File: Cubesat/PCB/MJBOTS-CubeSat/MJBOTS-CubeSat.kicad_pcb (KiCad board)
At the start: 2 copper layers, 88 x 73 mm, 11 parts, among them J1 Li 24V Battery, J2 MPU 6050, J3 Conn_01x08, J4 Conn_02x20_Odd_Even, U1 LM2596S

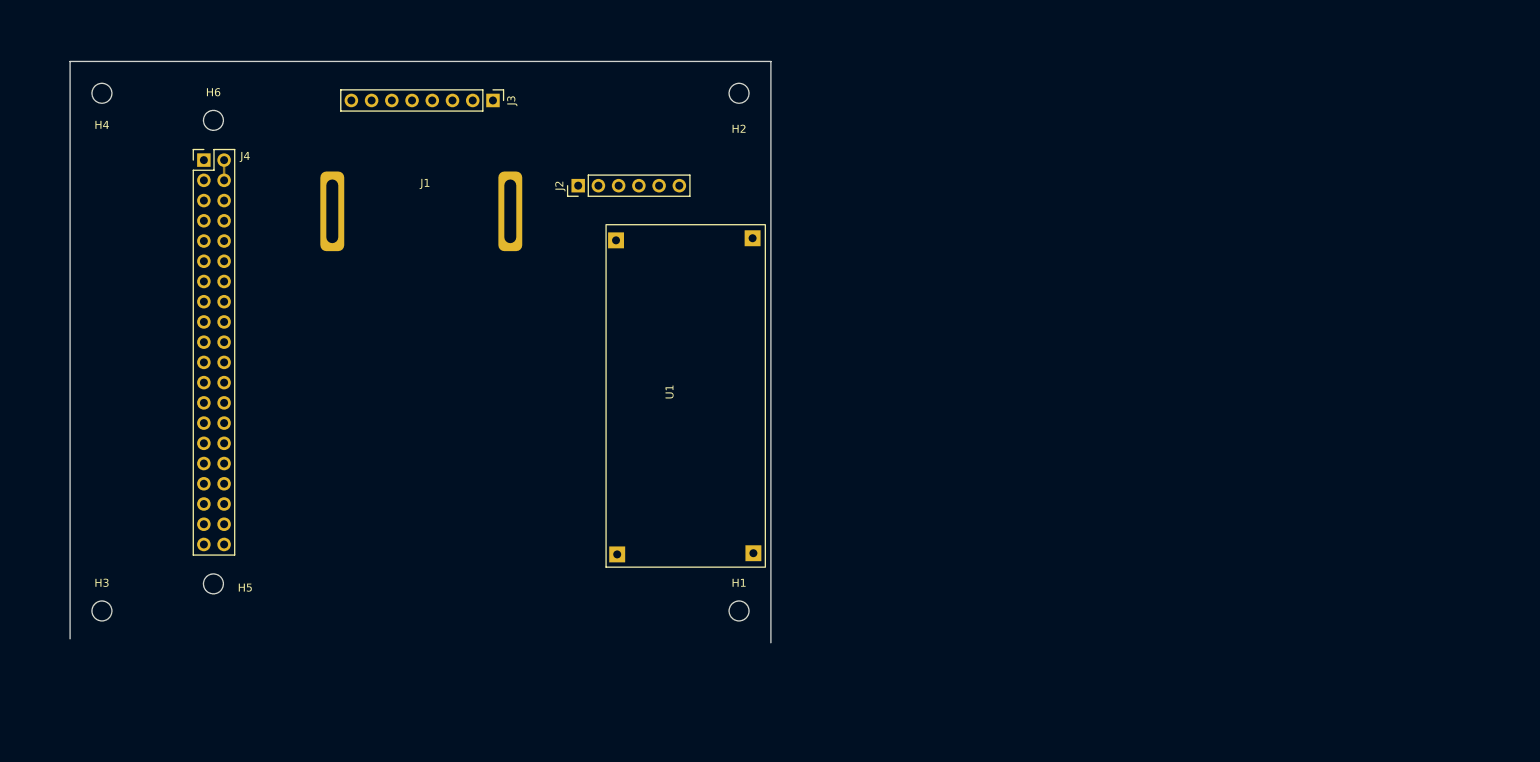
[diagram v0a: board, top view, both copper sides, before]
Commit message: Updated Moteus PCB
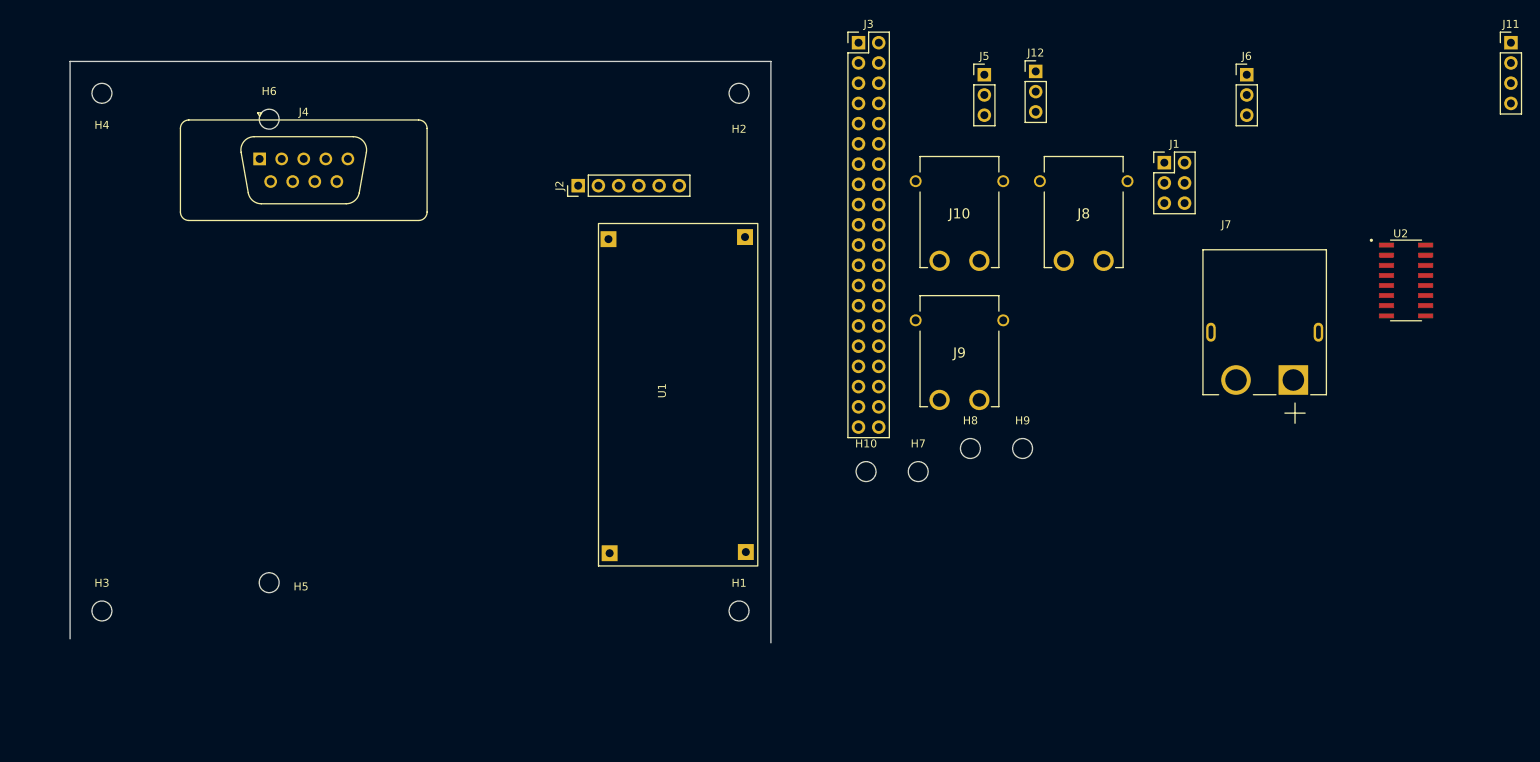
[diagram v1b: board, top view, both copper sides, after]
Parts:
- added H10: MountingHole, MountingHole:MountingHole_2.5mm, F.Cu at (194.9, 96.5)
- added H7: MountingHole, MountingHole:MountingHole_2.5mm, F.Cu at (201.5, 96.5)
- added H8: MountingHole, MountingHole:MountingHole_2.5mm, F.Cu at (208.1, 93.6)
- added H9: MountingHole, MountingHole:MountingHole_2.5mm, F.Cu at (214.6, 93.6)
- added J10: MOTOR3-XT30, cube:XT30PWM, F.Cu at (206.7, 64.1)
- added J11: JST-BATT, Connector_PinHeader_2.54mm:PinHeader_1x04_P2.54mm_Vertical, F.Cu at (275.9, 42.6)
- added J12: MOTOR3, Connector_PinHeader_2.54mm:PinHeader_1x03_P2.54mm_Vertical, F.Cu at (216.2, 46.2)
- added J5: MOTOR1, Connector_PinHeader_2.54mm:PinHeader_1x03_P2.54mm_Vertical, F.Cu at (209.8, 46.7)
- added J6: MOTOR2, Connector_PinHeader_2.54mm:PinHeader_1x03_P2.54mm_Vertical, F.Cu at (242.8, 46.7)
- added J7: INPUT-XT60, cube:AMASS_XT60PW-M, F.Cu at (245.0, 79.0)
- added J8: MOTOR1-XT30, cube:XT30PWM, F.Cu at (222.3, 64.1)
- added J9: MOTOR2-XT30, cube:XT30PWM, F.Cu at (206.7, 81.6)
- added U2: MCP3008-I/SL, cube:SOIC127P600X175-16N, F.Cu at (262.8, 72.5)
- J1: value Li 24V Battery -> Display; footprint cube:24V_Li_batt -> Connector_PinHeader_2.54mm:PinHeader_2x03_P2.54mm_Vertical
- J3: value Conn_01x08 -> Pi_GPIO; footprint Connector_PinHeader_2.54mm:PinHeader_1x08_P2.54mm_Vertical -> Connector_PinHeader_2.54mm:PinHeader_2x20_P2.54mm_Vertical
- J4: value Conn_02x20_Odd_Even -> CAN; footprint Connector_PinHeader_2.54mm:PinHeader_2x20_P2.54mm_Vertical -> Connector_Dsub:DSUB-9_Male_Vertical_P2.77x2.84mm
- moved J1 102.4 mm to (232.4, 57.7)
- moved J3 46.5 mm to (194.0, 42.6), turned to 0 degrees
- moved H5 7.00 mm to (120.0, 110.5)
- moved H6 7.00 mm to (120.0, 52.2)
- moved J4 7.00 mm to (118.8, 57.2)
- moved U1 0.96 mm to (171.2, 86.2)
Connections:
- J3 pad 1: VCC -> /3.3V
- J3 pad 2: GND -> /5V
- J3 pad 3: /brake -> /SDA
- J3 pad 4: /PWM -> /5V
- J3 pad 5: /CW/CCW -> /SCL
- J3 pad 6: unconnected-(J3-Pad6) -> GND
- J3 pad 7: /CHB -> unconnected-(J3-Pad7)
- J3 pad 8: /CHA -> unconnected-(J3-Pad8)
- J4 pad 1: /3.3V -> unconnected-(J4-Pad1)
- J4 pad 2: /5VB -> /CAN_L
- J4 pad 3: /SDA -> GND
- J4 pad 4: /5VB -> unconnected-(J4-Pad4)
- J4 pad 5: /SCL -> unconnected-(J4-Pad5)
- J4 pad 6: GND -> unconnected-(J4-Pad6)
- J4 pad 7: unconnected-(J4-Pad7) -> /CAN_H
- U1 pad 1: VCC -> /VCC
- U1 pad 3: /5VB -> /5V
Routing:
- net /5VB: track 2.54 -> 0.00 mm

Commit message: Updated CubeSat PCB
Still need the dimensions for the CAN bus converter
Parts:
- removed H5: MountingHole, MountingHole:MountingHole_2.5mm
- U2: moved to B.Cu
- moved J11 170.0 mm to (106.0, 47.6), turned to 90 degrees
- moved U2 155.2 mm to (107.7, 80.2), turned to -90 degrees
- moved J1 126.2 mm to (118.9, 112.9)
- moved J7 112.4 mm to (135.0, 56.1)
- moved J6 100.2 mm to (167.3, 112.6), turned to -90 degrees
- moved J10 87.6 mm to (133.9, 112.9), turned to 180 degrees
- moved J12 86.8 mm to (167.3, 118.0), turned to -90 degrees
- moved J8 86.3 mm to (151.2, 113.0), turned to 180 degrees
- moved J3 76.4 mm to (118.9, 57.1)
- moved H7 72.6 mm to (129.8, 84.8)
- moved H10 65.1 mm to (129.9, 97.0)
- moved J9 61.0 mm to (152.5, 53.6)
- moved H9 59.5 mm to (155.2, 97.5)
- moved H8 53.5 mm to (155.2, 85.3)
- moved J5 39.2 mm to (170.6, 47.9), turned to -90 degrees
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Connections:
- J3 pad 22: /CS -> unconnected-(J3-Pad22)
- J3 pad 24: /SCLK -> /CS
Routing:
- net /3.3V: track 0.00 -> 130.4 mm
- net /SDA: track 0.00 -> 123.0 mm
- net /SCL: track 0.00 -> 120.9 mm
- net /5V: track 0.00 -> 103.4 mm
- net /CAN_H: track 0.00 -> 94.2 mm
- net /CAN_L: track 0.00 -> 92.3 mm
- net /VCC: track 0.00 -> 89.1 mm
- net /A-D Converter/VT: track 0.00 -> 32.9 mm
- net /A-D Converter/CELL3: track 0.00 -> 32.3 mm
- net /A-D Converter/CELL1: track 0.00 -> 32.1 mm
- net /A-D Converter/CELL2: track 0.00 -> 31.8 mm
- net GND: track 0.00 -> 26.8 mm, vias 0 -> 1
- net /CS: track 0.00 -> 13.7 mm, vias 0 -> 1
- net /SCLK: track 0.00 -> 13.5 mm
- net /MISO: track 0.00 -> 13.3 mm
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- added copper zone on F.Cu, net GND
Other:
- board size 88 x 73 mm -> 88.1 x 76.3 mm

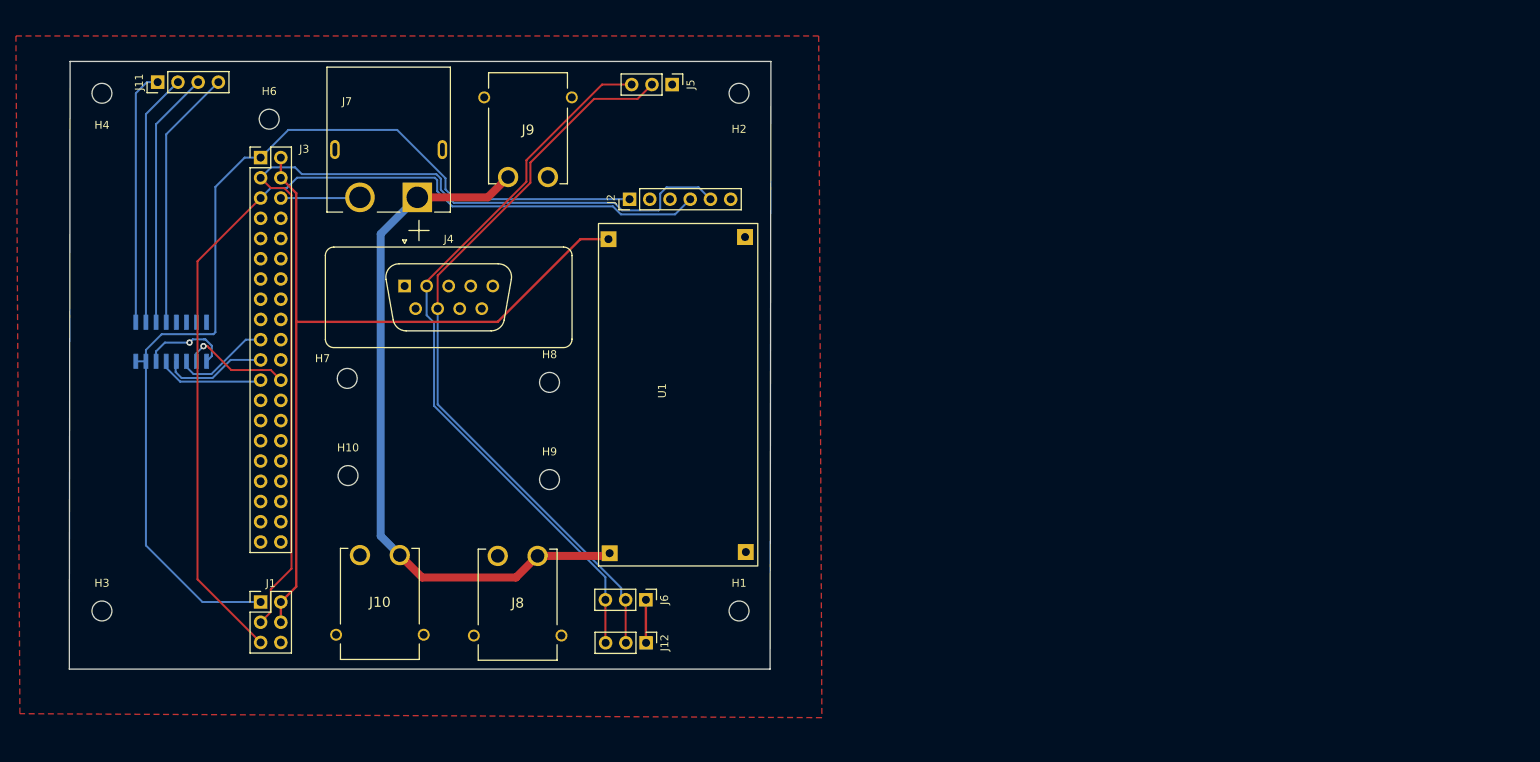
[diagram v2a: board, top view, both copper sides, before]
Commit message: Updated CubeSat PCB
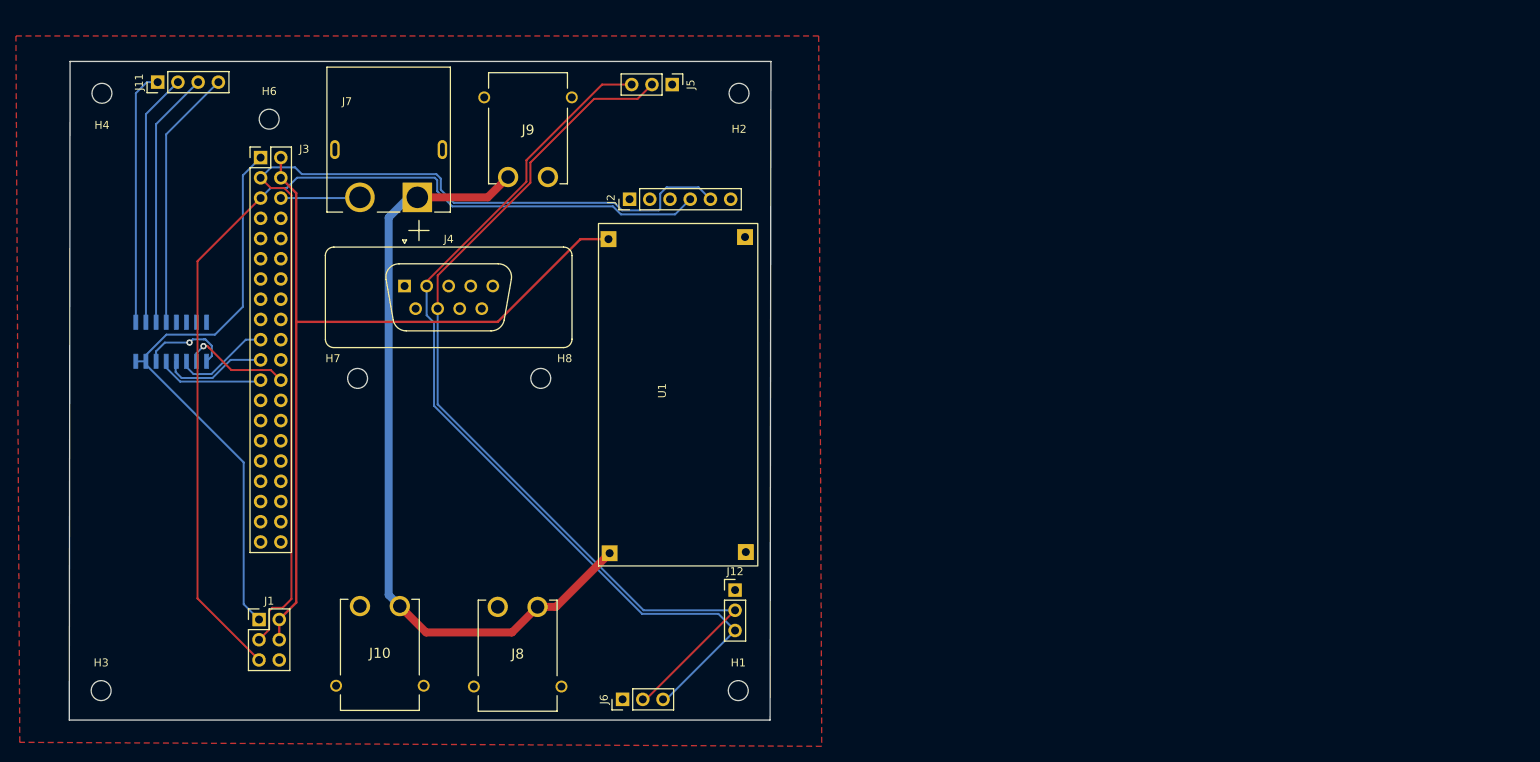
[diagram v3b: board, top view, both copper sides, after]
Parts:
- removed H10, H9: MountingHole, MountingHole:MountingHole_2.5mm
- moved J12 13.0 mm to (178.5, 111.4), turned to 0 degrees
- moved J6 12.8 mm to (164.4, 125.1), turned to 90 degrees
- moved H1 10.0 mm to (178.9, 124.0)
- moved H3 10.0 mm to (98.9, 124.0)
- moved J8 6.40 mm to (151.2, 119.4)
- moved J10 6.40 mm to (133.9, 119.3)
- moved J1 2.21 mm to (118.7, 115.1)
- moved H7 1.30 mm to (131.1, 84.8)
- moved H8 1.21 mm to (154.1, 84.8)
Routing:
- net /3.3V: track 130.4 -> 74.7 mm
- net /CAN_H: track 94.2 -> 118.8 mm
- net /CAN_L: track 92.3 -> 115.7 mm
- net /VCC: track 89.1 -> 98.3 mm
- net GND: track 26.8 -> 21.4 mm
- net /SDA: track 123.0 -> 126.1 mm
- net /5V: track 103.4 -> 105.7 mm
- net /SCL: track 120.9 -> 123.0 mm
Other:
- board size 88.1 x 76.3 mm -> 88.1 x 82.7 mm

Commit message: Finished CubeSat PCB
Uploaded gerber.zip
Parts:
- added H7: MountingHole, MountingHole:MountingHole_2.5mm, F.Cu at (129.7, 107.7)
- added H8: MountingHole, MountingHole:MountingHole_2.5mm, F.Cu at (154.7, 107.7)
- moved J4 11.1 mm to (147.7, 76.0), turned to 180 degrees
- moved H7 1.41 mm to (129.7, 84.6)
- moved H8 0.63 mm to (154.7, 84.6)
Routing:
- net /3.3V: track 74.7 -> 125.1 mm
- net /CAN_H: track 118.8 -> 113.9 mm
- net /VCC: track 98.3 -> 97.5 mm
- net /A-D Converter/CELL1: track 32.1 -> 31.3 mm
